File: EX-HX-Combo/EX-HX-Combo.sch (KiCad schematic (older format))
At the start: 46 parts, among them CN1 DB9 Male, J1 IDE_CONNECTOR, J200 Bus_Tandy_Plus_Through, J3 Bus_Tandy_Plus, SW1 SW_DIP_x10, U1 BIOS FLASH, U2 74HCT245, U3 1.8432 MHz, U4 DS1315, U5 AS6C4008-55PCN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

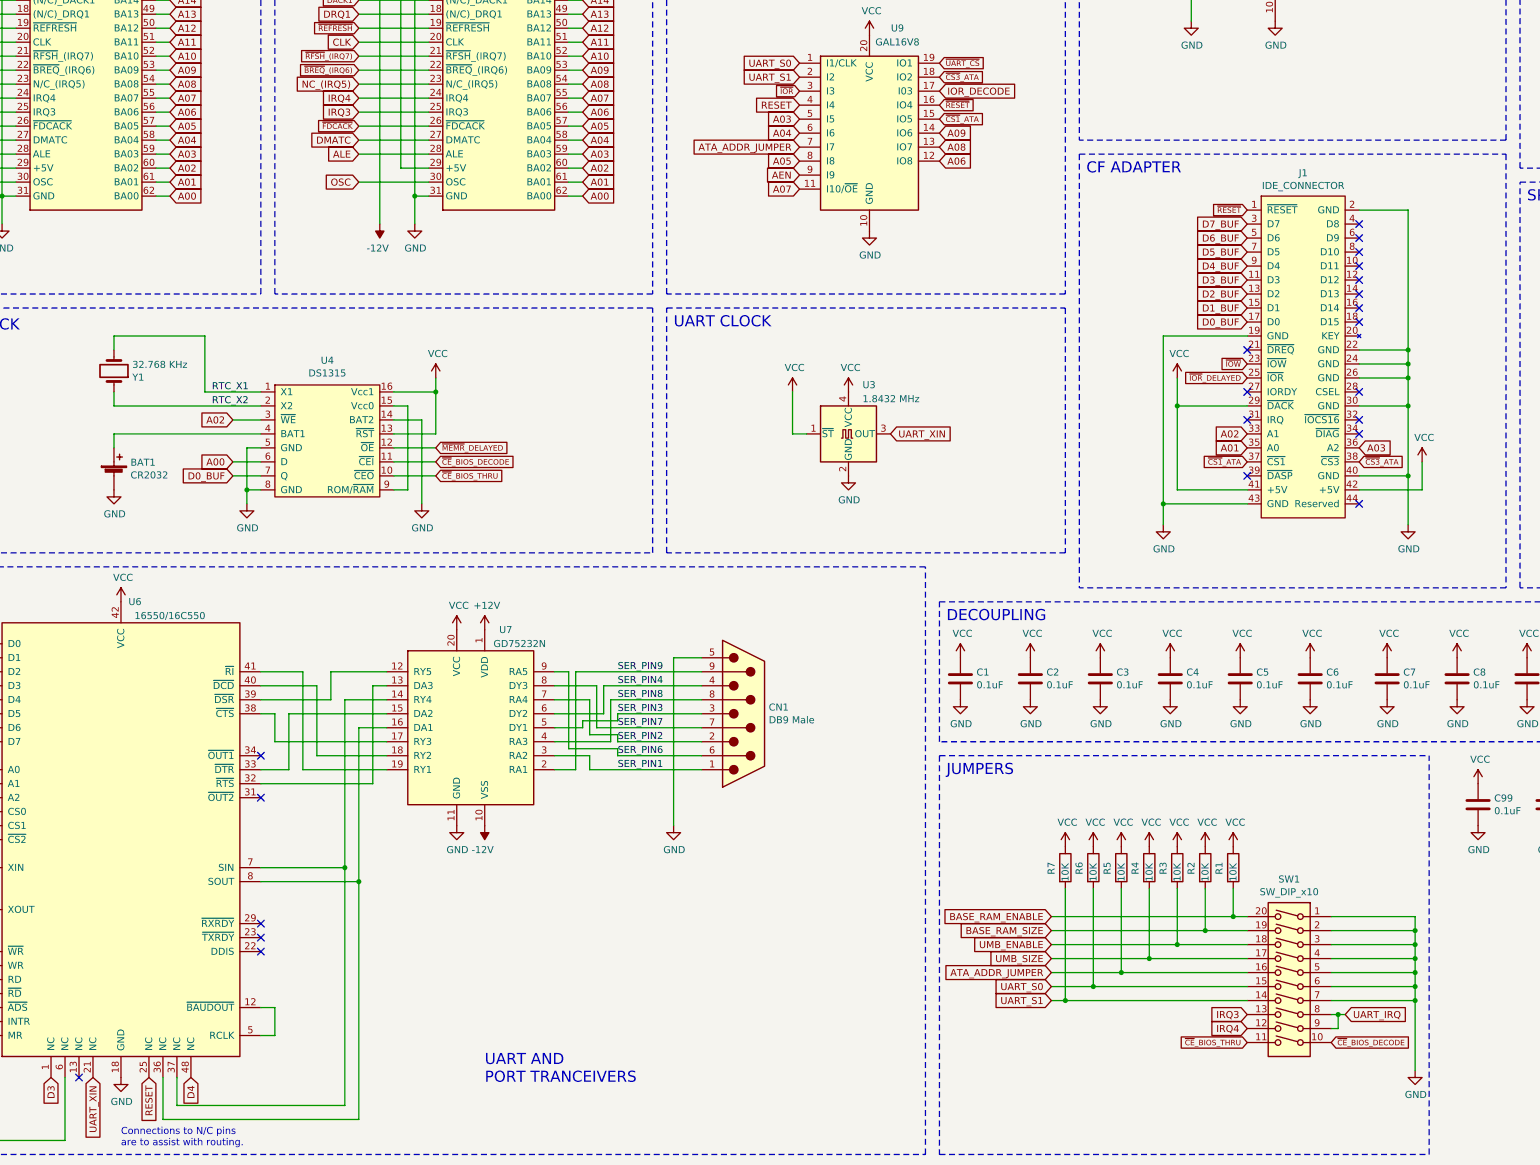
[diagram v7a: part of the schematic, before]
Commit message: Reorder dip switches on EX-HX-Combo.
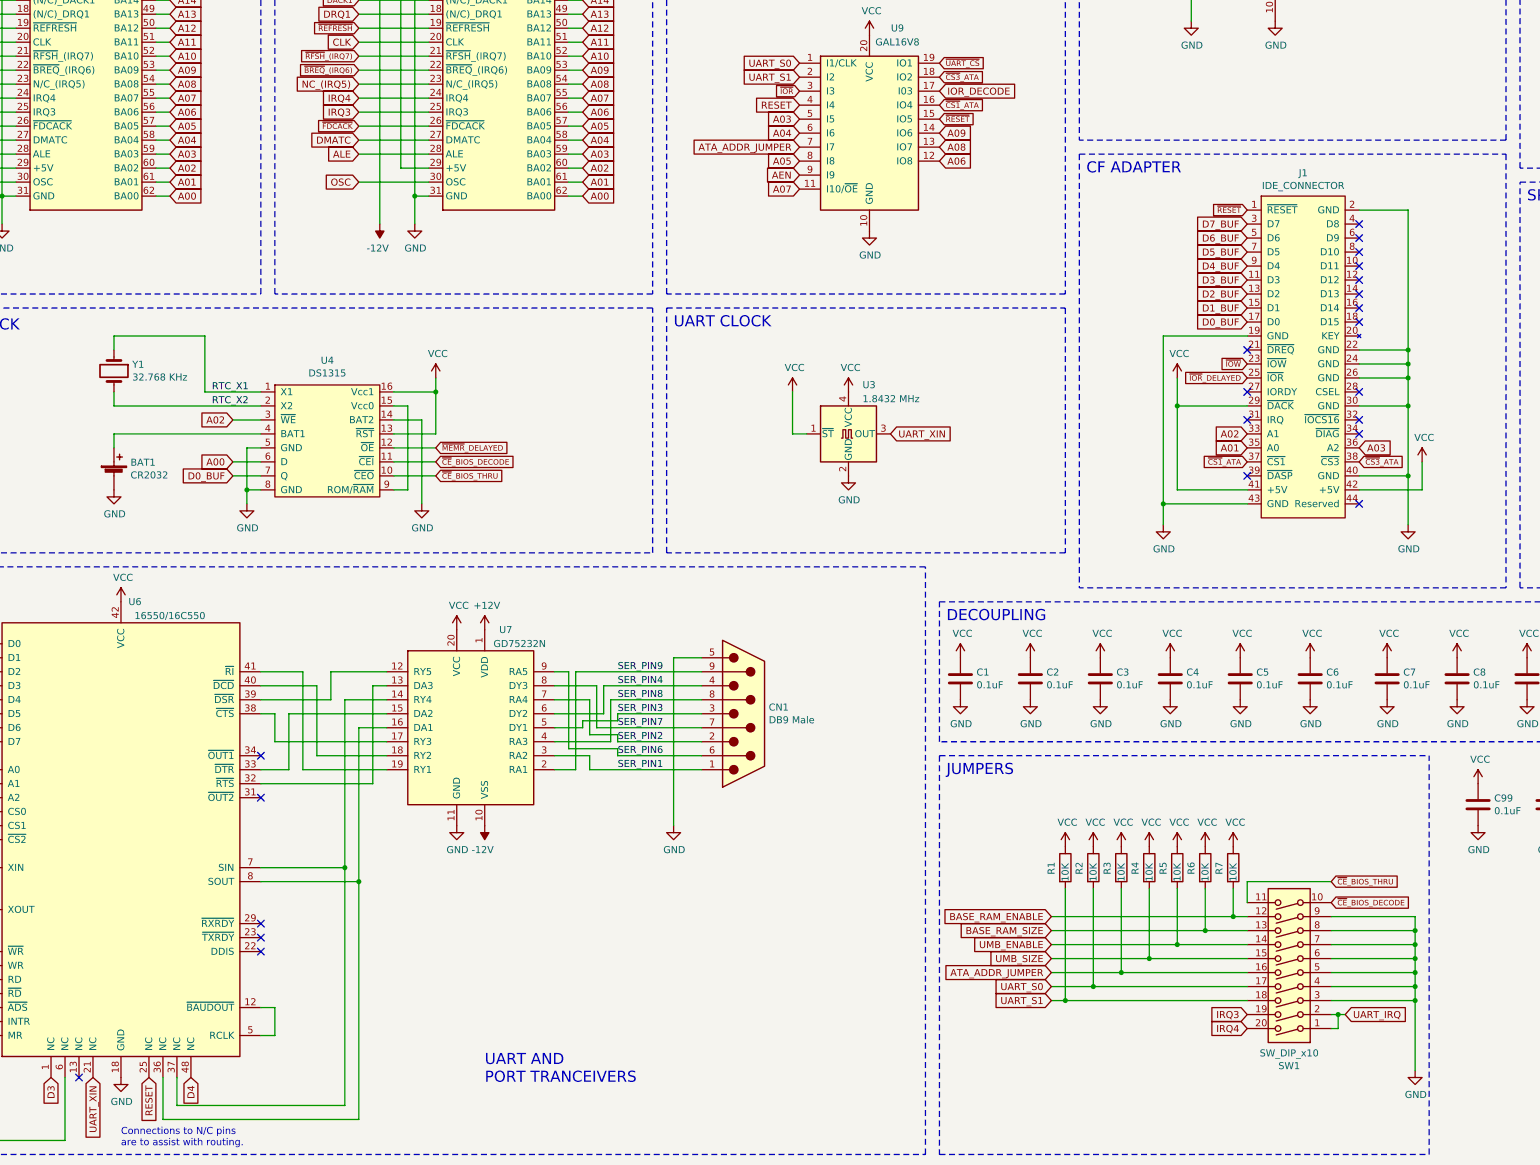
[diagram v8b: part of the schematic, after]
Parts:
- renumbered R7 to R1, R6 to R2, R5 to R3, R3 to R5, R2 to R6, R1 to R7
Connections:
- net BASE_RAM_ENABLE: now also SW1.12; no longer SW1.20
- net BASE_RAM_SIZE: now also SW1.13; no longer SW1.19
- net GND: now also SW1.8, SW1.9; no longer SW1.1, SW1.2
- net IRQ3: now also SW1.19; no longer SW1.13
- net IRQ4: now also SW1.20; no longer SW1.12
- net RTC_X1: now also Y1.1; no longer Y1.2
- net RTC_X2: now also Y1.2; no longer Y1.1
- net UART_IRQ: now also SW1.1, SW1.2; no longer SW1.8, SW1.9
- net UART_S0: now also SW1.17; no longer SW1.15
- net UART_S1: now also SW1.18; no longer SW1.14
- net UMB_ENABLE: now also SW1.14; no longer SW1.18
- net UMB_SIZE: now also SW1.15; no longer SW1.17
- net ~CS1~_ATA: now also U9.16 (IO4); no longer U9.15 (IO5)
- net ~RESET: now also U9.15 (IO5); no longer U9.16 (IO4)
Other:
- moved on the sheet: SW1
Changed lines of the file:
@@
 F 3 "~" H 2300 5500 50  0001 C CNN
 	1    2300 5500
-	0    1    -1   0
+	0    1    1    0
 $EndComp
 Wire Wire Line
@@
 Text GLabel 7200 3400 0    50   Input ~ 0
 UART_S1
-Text GLabel 8200 3700 2    39   Input ~ 0
+Text GLabel 8200 3600 2    39   Input ~ 0
 ~CS1~_ATA
 Text GLabel 8200 3300 2    39   Input ~ 0
@@
 Text GLabel 7200 3600 0    50   Input ~ 0
 RESET
-Text GLabel 8200 3600 2    39   Input ~ 0
+Text GLabel 8200 3700 2    39   Input ~ 0
 ~RESET
 Text GLabel 7200 1550 0    50   Input ~ 0
@@
 $EndComp
 $Comp
-L Device:R R7
+L Device:R R1
 U 1 1 60F85D03
 P 9100 9050
-F 0 "R7" V 9000 9000 50  0000 L CNN
+F 0 "R1" V 9000 9000 50  0000 L CNN
 F 1 "10K" V 9100 8950 50  0000 L CNN
 F 2 "Resistor_SMD:R_1206_3216Metric" V 9030 9050 50  0001 C CNN
@@
 Wire Wire Line
 	10300 9400 10300 9200
-$Comp
-L Device:R R1
-U 1 1 60EE41E5
-P 10300 9050
-F 0 "R1" V 10200 9000 50  0000 L CNN
-F 1 "10K" V 10300 8950 50  0000 L CNN
-F 2 "Resistor_SMD:R_1206_3216Metric" V 10230 9050 50  0001 C CNN
-F 3 "~" H 10300 9050 50  0001 C CNN
-	1    10300 9050
-	1    0    0    -1
-$EndComp
 $Comp
 L power:VCC #PWR0167
@@
 $EndComp
 $Comp
-L Device:R R5
+L Device:R R3
 U 1 1 60FB795F
 P 9500 9050
-F 0 "R5" V 9400 9000 50  0000 L CNN
+F 0 "R3" V 9400 9000 50  0000 L CNN
 F 1 "10K" V 9500 8950 50  0000 L CNN
 F 2 "Resistor_SMD:R_1206_3216Metric" V 9430 9050 50  0001 C CNN
@@
 $EndComp
 $Comp
-L Device:R R6
+L Device:R R2
 U 1 1 60FB7969
 P 9300 9050
-F 0 "R6" V 9200 9000 50  0000 L CNN
+F 0 "R2" V 9200 9000 50  0000 L CNN
 F 1 "10K" V 9300 8950 50  0000 L CNN
 F 2 "Resistor_SMD:R_1206_3216Metric" V 9230 9050 50  0001 C CNN
@@
 $EndComp
 $Comp
-L Device:R R3
-U 1 1 60FC7AA6
-P 9900 9050
-F 0 "R3" V 9800 9000 50  0000 L CNN
-F 1 "10K" V 9900 8950 50  0000 L CNN
-F 2 "Resistor_SMD:R_1206_3216Metric" V 9830 9050 50  0001 C CNN
-F 3 "~" H 9900 9050 50  0001 C CNN
-	1    9900 9050
-	1    0    0    -1
-$EndComp
-$Comp
 L Device:R R4
 U 1 1 60FC7AB0
@@
 $EndComp
 $Comp
-L Device:R R2
+L Device:R R6
 U 1 1 60FC7AD8
 P 10100 9050
-F 0 "R2" V 10000 9000 50  0000 L CNN
+F 0 "R6" V 10000 9000 50  0000 L CNN
 F 1 "10K" V 10100 8950 50  0000 L CNN
 F 2 "Resistor_SMD:R_1206_3216Metric" V 10030 9050 50  0001 C CNN
@@
 L Switch:SW_DIP_x10 SW1
 U 1 1 60DCA93E
-P 10700 9900
-F 0 "SW1" H 10700 10667 50  0000 C CNN
-F 1 "SW_DIP_x10" H 10700 10576 50  0000 C CNN
-F 2 "Button_Switch_THT:SW_DIP_SPSTx10_Slide_9.78x27.58mm_W7.62mm_P2.54mm" H 10700 9900 50  0001 C CNN
-F 3 "~" H 10700 9900 50  0001 C CNN
-	1    10700 9900
-	-1   0    0    -1
-$EndComp
-Text GLabel 11000 10300 2    39   Input ~ 0
+P 10700 9700
+F 0 "SW1" H 10700 10467 50  0000 C CNN
+F 1 "SW_DIP_x10" H 10700 10376 50  0000 C CNN
+F 2 "Button_Switch_THT:SW_DIP_SPSTx10_Slide_9.78x27.58mm_W7.62mm_P2.54mm" H 10700 9700 50  0001 C CNN
+F 3 "~" H 10700 9700 50  0001 C CNN
+	1    10700 9700
+	-1   0    0    1
+$EndComp
+Text GLabel 11000 9300 2    39   Input ~ 0
 ~CE~_BIOS_DECODE
-Text GLabel 10400 10300 0    39   Input ~ 0
+Text GLabel 11000 9150 2    39   Input ~ 0
 ~CE~_BIOS_THRU
 Wire Wire Line
@@
 Wire Wire Line
 	14550 9350 14550 9450
+Wire Wire Line
+	10400 9300 10400 9150
+Wire Wire Line
+	10400 9150 11000 9150
+$Comp
+L Device:R R7
+U 1 1 60EE41E5
+P 10300 9050
+F 0 "R7" V 10200 9000 50  0000 L CNN
+F 1 "10K" V 10300 8950 50  0000 L CNN
+F 2 "Resistor_SMD:R_1206_3216Metric" V 10230 9050 50  0001 C CNN
+F 3 "~" H 10300 9050 50  0001 C CNN
+	1    10300 9050
+	1    0    0    -1
+$EndComp
+$Comp
+L Device:R R5
+U 1 1 60FC7AA6
+P 9900 9050
+F 0 "R5" V 9800 9000 50  0000 L CNN
+F 1 "10K" V 9900 8950 50  0000 L CNN
+F 2 "Resistor_SMD:R_1206_3216Metric" V 9830 9050 50  0001 C CNN
+F 3 "~" H 9900 9050 50  0001 C CNN
+	1    9900 9050
+	1    0    0    -1
+$EndComp
 $EndSCHEMATC
